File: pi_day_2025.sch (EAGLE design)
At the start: 67 parts, among them IC1 W25Q64JVXGIQ, J4 SM03B-SRSS-TB(LF)(SN), Q2 BSS138, U1 APS6404L-3SQR-ZR, U2 RP2350A, U4 LTC4088EDE#PBF, Y1 12MHz

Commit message: File upload
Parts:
- added C14, C15: 10uF, SparkFun-Capacitors:10UF-0805-10V-10%
- added D11: BLUE, SparkFun-LED:LED-BLUE0603
- added Q1: Si2333, SparkFun-DiscreteSemi:MOSFET_PCH-SI2309DS
- Q2: value BSS138 -> 310mA/60V/1.6Ω
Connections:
- removed net NEOPIXEL: U2.GPIO16
- new net VBUS: CONN1.VBUS, Q1.D
- net 3.3V: now also C14.1, U4.LDO3V3, U4.VOUT
- net GND: now also C14.2, C15.2, D11.C, Q1.G, U4.GND
- net N$4: now also D11.A
- net N$9: now also Q1.S; no longer CONN1.VBUS
- net V_USB: now also C15.1, U4.VBUS
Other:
- note removed: "USB Power Supply"
- moved on the sheet: C12, C13, L1

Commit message: Check-in
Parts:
- added C16: 0.1uF, SparkFun-Capacitors:0.1UF-0402-6.3V-10%-X7R
- added C19: 0.1uF, SparkFun-Capacitors:0.1UF-0402T-16V-10%-X7R-WE
- added D12: 1N5819HW-7, 1N5819HW-7:1N5819HW-7
- added J1: (no value), SparkFun-Connectors:JST_2MM_MALE
- added L3: ASPI-0602S-3R3M-T, ASPI-0602S-3R3M-T:ASPI-0602S-3R3M-T
- added MK1: SPK2611HM7H-1-6, SPK2611HM7H-1-6:SPK2611HM7H-1-6
- added Q3: Si2333, SparkFun-DiscreteSemi:MOSFET_PCH-SI2309DS
- added R10: 2.94K, SparkFun-Resistors:RESISTOR0402
- added R14: 8.2, SparkFun-Resistors:RESISTOR0402
- added R16: 100K, SparkFun-Resistors:100KOHM-0402-1/16W-1%
- added R17: 100k, SparkFun-Resistors:NTC-THERMISTOR-0603
- added R9: 499, SparkFun-Resistors:RESISTOR0402
- added U3: TPS76318DBVRG4, TPS76318DBVRG4:TPS76318DBVRG4
- added U5: TXS0108EPWRG4, TXS0108EPWRG4:TXS0108EPWRG4
- added U6: LSM6DS3TR-C, LSM6DS3TR-C:LSM6DS3TR-C
- R3, R8: value 5.1K -> (none)
- R5: value 10K -> (none)
- R6, R7: value 2.2K -> (none)
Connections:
- new net 1.8V: MK1.VDD
- new net LSM6_INT1: U6.INT1
- new net LSM6_INT2: U6.INT2
- new net N$10: J1.+, Q3.D, U4.BAT
- new net N$14: R9.2, U4.C/X, U4.PROG
- new net N$15: R10.2, R14.2, U4.CLPROG
- new net N$16: C16.1, R14.1
- new net N$17: R16.1, R17.1, U4.NTC
- new net N$6: L3.P$2, U4.SW
- new net N$8: Q3.G, U4.GATE
- new net NPXL_1_IN: D1.DIN, U2.GPIO9
- new net NPXL_1_OUT: D1.DOUT, D2.DIN
- new net NPXL_2_OUT: D2.DOUT, D3.DIN
- new net NPXL_3_OUT: D3.DOUT, D4.DIN
- new net NPXL_4_OUT: D4.DOUT, D5.DIN
- new net NPXL_5_OUT: D5.DOUT, D6.DIN
- new net NPXL_6_OUT: D6.DOUT, D7.DIN
- new net NPXL_7_OUT: D7.DOUT, D8.DIN
- new net NPXL_8_OUT: D8.DOUT, D9.DIN
- new net NPXL_9_OUT: D10.DIN, D9.DOUT
- net 3.3V: now also C19.1, D12.K, L3.P$1, Q3.S, U6.CS, U6.SDO/SA0, U6.VDD, U6.VDDIO
- net GND: now also C16.2, C19.2, J1.-, MK1.GND, R10.1, R17.2, R9.1, U4.D0, U4.D2, U6.GND, U6.SCX, U6.SDX
- net N$26: now also D12.A
- net SCL: now also U6.SCL
- net SDA: now also U6.SDA
- net V_USB: now also R16.2, U4.D1
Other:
- note added: "LTC4088"
- note added: "USB"

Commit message: Check-in
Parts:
- removed L3: ASPI-0602S-3R3M-T, ASPI-0602S-3R3M-T:ASPI-0602S-3R3M-T
- removed Q1, Q3: Si2333, SparkFun-DiscreteSemi:MOSFET_PCH-SI2309DS
- added C20: 1.0uF, SparkFun-Capacitors:1.0UF-0402-16V-10%
- added D13, D14, D15: GREEN, SparkFun-LED:LED-GREEN0603
- added R18, R19: 220, SparkFun-Resistors:220OHM-0402-TIGHT-1/16W-1%
- added R20: 1K, SparkFun-Resistors:1KOHM-0402-1/16W-1%
- added U7: MCP73833T-AMI/MF, MCP73833T-AMI_MF:MCP73833T-AMI/MF
- added U8: TPS2113APWR, TPS2113APWR:TPS2113APWR
- C14, C15: value 10uF -> 0.1uF; device SparkFun-Capacitors:10UF-0805-10V-10% -> SparkFun-Capacitors:0.1UF-0402-10V-10%-X7R
- C16: value 0.1uF -> 1.0uF; device SparkFun-Capacitors:0.1UF-0402-6.3V-10%-X7R -> SparkFun-Capacitors:1.0UF-0402-16V-10%
- L1: value 3.9NH -> 2.2nH; device SparkFun-Coils:INDUCTOR-0402-3.9NH -> LQW18AN2N2D10D:LQW18AN2N2D10D
- R10: value 2.94K -> 100K; device SparkFun-Resistors:RESISTOR0402 -> SparkFun-Resistors:100KOHM-0402-1/16W-1%
- R14: value 8.2 -> 500
- R16: value 100K -> 220; device SparkFun-Resistors:100KOHM-0402-1/16W-1% -> SparkFun-Resistors:220OHM-0402-TIGHT-1/16W-1%
- R17: value 100k -> 10k
- R3, R8: value (none) -> 5.1K
- R4: value DNF -> (none)
- R9: value 499 -> 100K; device SparkFun-Resistors:RESISTOR0402 -> SparkFun-Resistors:100KOHM-0402-1/16W-1%
- U4: value LTC4088EDE#PBF -> TPS63001DRCR; device LTC4088EDE_PBF:LTC4088EDE#PBF -> TPS63001DRCR:TPS63001DRCR
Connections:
- new net CHARGE_STAT: U2.GPIO1, U7.STAT1
- new net N$18: D15.C, U7.STAT2
- new net N$19: R20.2, U7.PROG
- new net VIN: U8.OUT
- new net V_BATT: C15.1, C20.1, J1.+, U7.VBAT, U8.IN2
- net 3.3V: no longer C14.1, L3.P$1, Q3.S, U4.LDO3V3, U4.VOUT
- net GND: now also C14.1, C16.1, C20.2, R10.2, R14.1, R17.1, R20.1, U4.PGND, U4.POWER_PAD, U7.EXP, U7.VSS, U8.!EN, U8.GND; no longer C14.2, C16.2, Q1.G, R10.1, R17.2, R9.1, U4.D0, U4.D2
- net N$10: now also D13.C, U8.STAT; no longer J1.+, Q3.D, U4.BAT
- net N$14: now also R17.2, U7.THERM; no longer R9.2, U4.C/X, U4.PROG
- net N$15: now also D14.A, R18.1; no longer R10.2, R14.2, U4.CLPROG
- net N$16: now also D14.C, U7.!PG; no longer C16.1, R14.1
- net N$17: now also D15.A, R19.1; no longer R16.1, R17.1, U4.NTC
- net N$6: now also R10.1, R9.2, U8.VSNS; no longer L3.P$2, U4.SW
- net N$8: now also R14.2, U8.ILIM; no longer Q3.G, U4.GATE
- net N$9: now also D13.A, R16.1; no longer C12.1, L1.1, Q1.S
- net VBUS: now also C12.1, L1.1; no longer Q1.D
- net V_USB: now also C14.2, C16.2, R18.2, R19.2, R9.1, U7.VDD, U8.IN1; no longer C15.1, U4.D1, U4.VBUS
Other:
- note removed: "LTC4088"
- moved on the sheet: C12, C13, C14, C15, C16, CONN1, J1, L1, R10, R14, R16, R17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

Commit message: Finished power supply design
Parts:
- added C21, C22, C23: 10uF, SparkFun-Capacitors:10UF-0402T-6.3V-20%
- added C24: 0.1uF, SparkFun-Capacitors:0.1UF-0402-16V-10%
- added L3: LQH3NPN2R2MJRL, LQH3NPN2R2MJRL:LQH3NPN2R2MJRL
- added R21: 100, SparkFun-Resistors:100OHM-0402-TIGHT-1/16W-1%
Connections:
- new net N$20: L3.P$2, U4.L1
- new net N$21: L3.P$1, U4.L2
- new net N$22: C24.1, R21.1, U4.EN, U4.PS/SYNC, U4.VINA
- net 3.3V: now also C21.1, C22.1, U4.FB, U4.VOUT
- net GND: now also C21.2, C22.2, C23.2, C24.2
- net VIN: now also C23.1, R21.2, U4.VIN

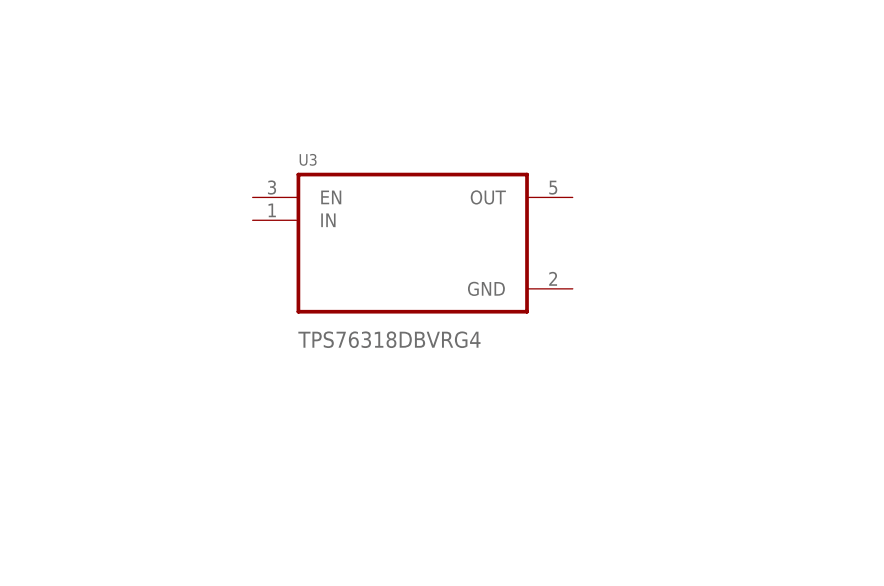
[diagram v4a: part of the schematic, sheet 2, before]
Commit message: Added 1.8V regulator
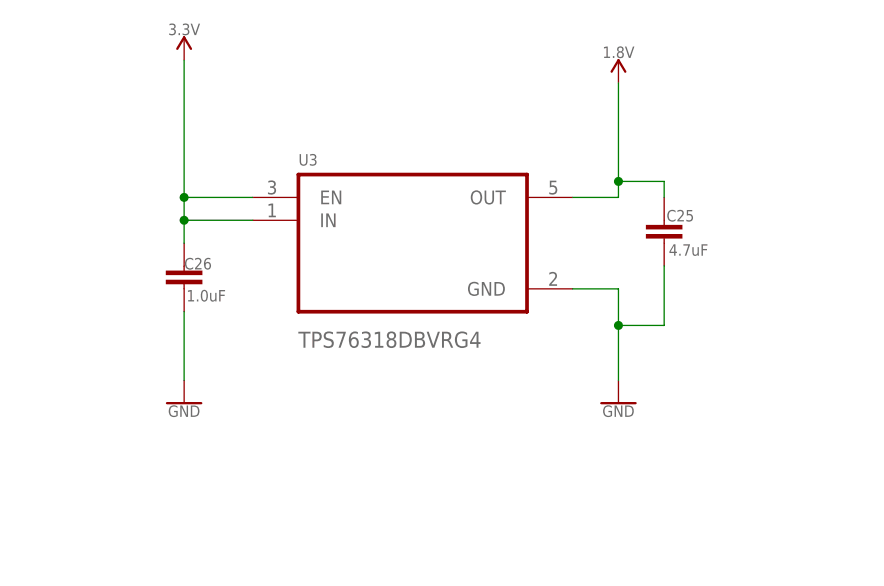
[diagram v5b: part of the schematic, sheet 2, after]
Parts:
- added C25: 4.7uF, SparkFun-Capacitors:4.7UF-0402_TIGHT-6.3V-20%-X5R
- added C26: 1.0uF, SparkFun-Capacitors:1.0UF-0402-16V-10%
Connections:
- net 1.8V: now also C25.1, U3.OUT
- net 3.3V: now also C26.1, U3.EN, U3.IN
- net GND: now also C25.2, C26.2, U3.GND
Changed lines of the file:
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@@
 <part name="C24" library="SparkFun-Capacitors" library_urn="urn:adsk.eagle:library:510" deviceset="0.1UF" device="-0402-16V-10%" package3d_urn="urn:adsk.eagle:package:41385089/1" override_package3d_urn="urn:adsk.eagle:package:44163386/2" override_package_urn="urn:adsk.eagle:footprint:37389/1" override_locally_modified="yes" value="0.1uF"/>
 <part name="GND44" library="SparkFun-PowerSymbols" library_urn="urn:adsk.eagle:library:530" deviceset="GND" device=""/>
+<part name="GND45" library="SparkFun-PowerSymbols" library_urn="urn:adsk.eagle:library:530" deviceset="GND" device=""/>
+<part name="SUPPLY32" library="SparkFun-PowerSymbols" library_urn="urn:adsk.eagle:library:530" deviceset="1.8V" device=""/>
+<part name="C25" library="SparkFun-Capacitors" library_urn="urn:adsk.eagle:library:510" deviceset="4.7UF" device="-0402_TIGHT-6.3V-20%-X5R" package3d_urn="urn:adsk.eagle:package:41385069/1" value="4.7uF"/>
+<part name="SUPPLY33" library="SparkFun-PowerSymbols" library_urn="urn:adsk.eagle:library:530" deviceset="3.3V" device=""/>
+<part name="C26" library="SparkFun-Capacitors" library_urn="urn:adsk.eagle:library:510" deviceset="1.0UF" device="-0402-16V-10%" package3d_urn="urn:adsk.eagle:package:41385089/1" value="1.0uF"/>
+<part name="GND46" library="SparkFun-PowerSymbols" library_urn="urn:adsk.eagle:library:530" deviceset="GND" device=""/>
 </parts>
 <sheets>
@@
 <attribute name="VALUE" x="248.158" y="53.848" size="1.27" layer="96" font="vector" ratio="20" rot="R180"/>
 </instance>
+<instance part="GND45" gate="1" x="200.66" y="129.54" smashed="yes">
+<attribute name="VALUE" x="200.66" y="129.286" size="1.27" layer="96" font="vector" ratio="20" align="top-center"/>
+</instance>
+<instance part="SUPPLY32" gate="G$1" x="200.66" y="165.1" smashed="yes">
+<attribute name="VALUE" x="200.66" y="167.894" size="1.27" layer="96" font="vector" ratio="20" align="bottom-center"/>
+</instance>
+<instance part="C25" gate="G$1" x="205.74" y="147.32" smashed="yes">
+<attribute name="NAME" x="205.994" y="149.733" size="1.27" layer="95" font="vector" ratio="20"/>
+<attribute name="VALUE" x="206.248" y="145.923" size="1.27" layer="96" font="vector" ratio="20"/>
+</instance>
+<instance part="SUPPLY33" gate="G$1" x="152.4" y="167.64" smashed="yes">
+<attribute name="VALUE" x="152.4" y="170.434" size="1.27" layer="96" font="vector" ratio="20" align="bottom-center"/>
+</instance>
+<instance part="C26" gate="G$1" x="152.4" y="142.24" smashed="yes">
+<attribute name="NAME" x="152.4" y="144.399" size="1.27" layer="95" font="vector" ratio="20"/>
+<attribute name="VALUE" x="152.654" y="140.843" size="1.27" layer="96" font="vector" ratio="20"/>
+</instance>
+<instance part="GND46" gate="1" x="152.4" y="129.54" smashed="yes">
+<attribute name="VALUE" x="152.4" y="129.286" size="1.27" layer="96" font="vector" ratio="20" align="top-center"/>
+</instance>
 </instances>
 <busses>
@@
 <wire x1="256.54" y1="25.4" x2="256.54" y2="32.258" width="0.1524" layer="91"/>
 </segment>
+<segment>
+<pinref part="GND45" gate="1" pin="GND"/>
+<pinref part="U3" gate="A" pin="GND"/>
+<wire x1="200.66" y1="132.08" x2="200.66" y2="138.176" width="0.1524" layer="91"/>
+<wire x1="200.66" y1="138.176" x2="200.66" y2="142.24" width="0.1524" layer="91"/>
+<wire x1="200.66" y1="142.24" x2="195.58" y2="142.24" width="0.1524" layer="91"/>
+<pinref part="C25" gate="G$1" pin="2"/>
+<wire x1="205.74" y1="144.78" x2="205.74" y2="138.176" width="0.1524" layer="91"/>
+<wire x1="205.74" y1="138.176" x2="200.66" y2="138.176" width="0.1524" layer="91"/>
+<junction x="200.66" y="138.176"/>
+</segment>
+<segment>
+<pinref part="C26" gate="G$1" pin="2"/>
+<pinref part="GND46" gate="1" pin="GND"/>
+<wire x1="152.4" y1="132.08" x2="152.4" y2="139.7" width="0.1524" layer="91"/>
+</segment>
 </net>
 <net name="1.8V" class="0">
@@
 <wire x1="73.66" y1="154.94" x2="81.28" y2="154.94" width="0.1524" layer="91"/>
 <wire x1="81.28" y1="154.94" x2="81.28" y2="167.64" width="0.1524" layer="91"/>
+</segment>
+<segment>
+<pinref part="U3" gate="A" pin="OUT"/>
+<pinref part="SUPPLY32" gate="G$1" pin="1.8V"/>
+<wire x1="195.58" y1="152.4" x2="200.66" y2="152.4" width="0.1524" layer="91"/>
+<wire x1="200.66" y1="152.4" x2="200.66" y2="154.178" width="0.1524" layer="91"/>
+<pinref part="C25" gate="G$1" pin="1"/>
+<wire x1="200.66" y1="154.178" x2="200.66" y2="165.1" width="0.1524" layer="91"/>
+<wire x1="205.74" y1="152.4" x2="205.74" y2="154.178" width="0.1524" layer="91"/>
+<wire x1="205.74" y1="154.178" x2="200.66" y2="154.178" width="0.1524" layer="91"/>
+<junction x="200.66" y="154.178"/>
 </segment>
 </net>
@@
 <wire x1="248.666" y1="61.214" x2="248.666" y2="66.04" width="0.1524" layer="91"/>
 </segment>
-</net>
+<segment>
+<pinref part="U3" gate="A" pin="IN"/>
+<pinref part="SUPPLY33" gate="G$1" pin="3.3V"/>
+<wire x1="160.02" y1="149.86" x2="152.4" y2="149.86" width="0.1524" layer="91"/>
+<wire x1="152.4" y1="149.86" x2="152.4" y2="152.4" width="0.1524" layer="91"/>
+<pinref part="U3" gate="A" pin="EN"/>
+<wire x1="152.4" y1="152.4" x2="152.4" y2="167.64" width="0.1524" layer="91"/>
+<wire x1="160.02" y1="152.4" x2="152.4" y2="152.4" width="0.1524" layer="91"/>
+<junction x="152.4" y="152.4"/>
+<pinref part="C26" gate="G$1" pin="1"/>
+<wire x1="152.4" y1="147.32" x2="152.4" y2="149.86" width="0.1524" layer="91"/>
+<junction x="152.4" y="149.86"/>
+</segment>
+</net>

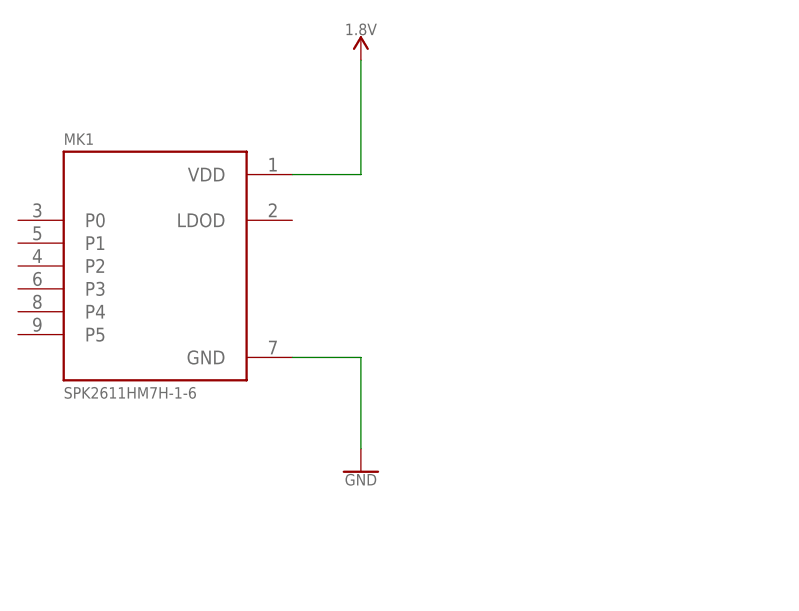
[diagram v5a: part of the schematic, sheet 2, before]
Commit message: Added bypass capacitor to IA611
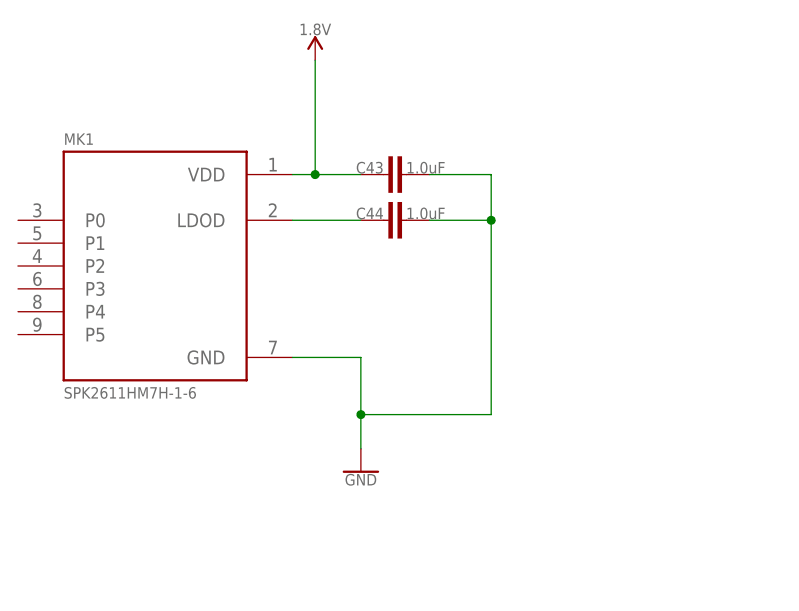
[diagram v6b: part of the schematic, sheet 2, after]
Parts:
- added C43, C44: 1.0uF, SparkFun-Capacitors:1.0UF-0402-16V-10%
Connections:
- new net N$23: C44.1, MK1.LDOD
- net 1.8V: now also C43.1
- net GND: now also C43.2, C44.2
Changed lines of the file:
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@@
 <part name="C26" library="SparkFun-Capacitors" library_urn="urn:adsk.eagle:library:510" deviceset="1.0UF" device="-0402-16V-10%" package3d_urn="urn:adsk.eagle:package:41385089/1" value="1.0uF"/>
 <part name="GND46" library="SparkFun-PowerSymbols" library_urn="urn:adsk.eagle:library:530" deviceset="GND" device=""/>
+<part name="C43" library="SparkFun-Capacitors" library_urn="urn:adsk.eagle:library:510" deviceset="1.0UF" device="-0402-16V-10%" package3d_urn="urn:adsk.eagle:package:41385089/1" value="1.0uF"/>
+<part name="C44" library="SparkFun-Capacitors" library_urn="urn:adsk.eagle:library:510" deviceset="1.0UF" device="-0402-16V-10%" package3d_urn="urn:adsk.eagle:package:41385089/1" value="1.0uF"/>
 </parts>
 <sheets>
@@
 <attribute name="VALUE" x="81.28" y="121.666" size="1.27" layer="96" font="vector" ratio="20" align="top-center"/>
 </instance>
-<instance part="SUPPLY20" gate="G$1" x="81.28" y="167.64" smashed="yes">
-<attribute name="VALUE" x="81.28" y="170.434" size="1.27" layer="96" font="vector" ratio="20" align="bottom-center"/>
+<instance part="SUPPLY20" gate="G$1" x="76.2" y="167.64" smashed="yes">
+<attribute name="VALUE" x="76.2" y="170.434" size="1.27" layer="96" font="vector" ratio="20" align="bottom-center"/>
 </instance>
 <instance part="U3" gate="A" x="177.8" y="147.32" smashed="yes">
@@
 <instance part="GND46" gate="1" x="152.4" y="129.54" smashed="yes">
 <attribute name="VALUE" x="152.4" y="129.286" size="1.27" layer="96" font="vector" ratio="20" align="top-center"/>
+</instance>
+<instance part="C43" gate="G$1" x="86.36" y="154.94" smashed="yes" rot="R90">
+<attribute name="NAME" x="83.82" y="156.337" size="1.27" layer="95" font="vector" ratio="20" rot="R180"/>
+<attribute name="VALUE" x="90.678" y="156.337" size="1.27" layer="96" font="vector" ratio="20" rot="R180"/>
+</instance>
+<instance part="C44" gate="G$1" x="86.36" y="149.86" smashed="yes" rot="R90">
+<attribute name="NAME" x="83.82" y="151.257" size="1.27" layer="95" font="vector" ratio="20" rot="R180"/>
+<attribute name="VALUE" x="90.678" y="151.257" size="1.27" layer="96" font="vector" ratio="20" rot="R180"/>
 </instance>
 </instances>
@@
 <pinref part="GND32" gate="1" pin="GND"/>
 <pinref part="MK1" gate="G$1" pin="GND"/>
-<wire x1="81.28" y1="124.46" x2="81.28" y2="134.62" width="0.1524" layer="91"/>
+<wire x1="81.28" y1="124.46" x2="81.28" y2="128.27" width="0.1524" layer="91"/>
+<wire x1="81.28" y1="128.27" x2="81.28" y2="134.62" width="0.1524" layer="91"/>
 <wire x1="81.28" y1="134.62" x2="73.66" y2="134.62" width="0.1524" layer="91"/>
+<pinref part="C43" gate="G$1" pin="2"/>
+<wire x1="88.9" y1="154.94" x2="95.758" y2="154.94" width="0.1524" layer="91"/>
+<wire x1="95.758" y1="154.94" x2="95.758" y2="149.86" width="0.1524" layer="91"/>
+<wire x1="95.758" y1="149.86" x2="95.758" y2="128.27" width="0.1524" layer="91"/>
+<wire x1="95.758" y1="128.27" x2="81.28" y2="128.27" width="0.1524" layer="91"/>
+<junction x="81.28" y="128.27"/>
+<pinref part="C44" gate="G$1" pin="2"/>
+<wire x1="88.9" y1="149.86" x2="95.758" y2="149.86" width="0.1524" layer="91"/>
+<junction x="95.758" y="149.86"/>
 </segment>
 <segment>
@@
 <pinref part="MK1" gate="G$1" pin="VDD"/>
 <pinref part="SUPPLY20" gate="G$1" pin="1.8V"/>
-<wire x1="73.66" y1="154.94" x2="81.28" y2="154.94" width="0.1524" layer="91"/>
-<wire x1="81.28" y1="154.94" x2="81.28" y2="167.64" width="0.1524" layer="91"/>
+<wire x1="73.66" y1="154.94" x2="76.2" y2="154.94" width="0.1524" layer="91"/>
+<wire x1="76.2" y1="154.94" x2="76.2" y2="167.64" width="0.1524" layer="91"/>
+<pinref part="C43" gate="G$1" pin="1"/>
+<wire x1="81.28" y1="154.94" x2="76.2" y2="154.94" width="0.1524" layer="91"/>
+<junction x="76.2" y="154.94"/>
 </segment>
 <segment>
@@
 </segment>
 </net>
+<net name="N$23" class="0">
+<segment>
+<pinref part="MK1" gate="G$1" pin="LDOD"/>
+<pinref part="C44" gate="G$1" pin="1"/>
+<wire x1="73.66" y1="149.86" x2="81.28" y2="149.86" width="0.1524" layer="91"/>
+</segment>
+</net>
